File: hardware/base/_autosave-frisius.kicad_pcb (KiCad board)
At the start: 4 copper layers, 46 x 85 mm, 124 parts, among them J1 MEM2067, J2 USB_C_Receptacle_USB2.0, J3 BATTERY, J4 Debug UART, J5 Conn_02x16_Odd_Even_MountingP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, J7 I2C ISENSE, Q2 Q_NMOS_DGS, Q3 Q_NMOS_DGS, SW1 RESET, SW2 BOOT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

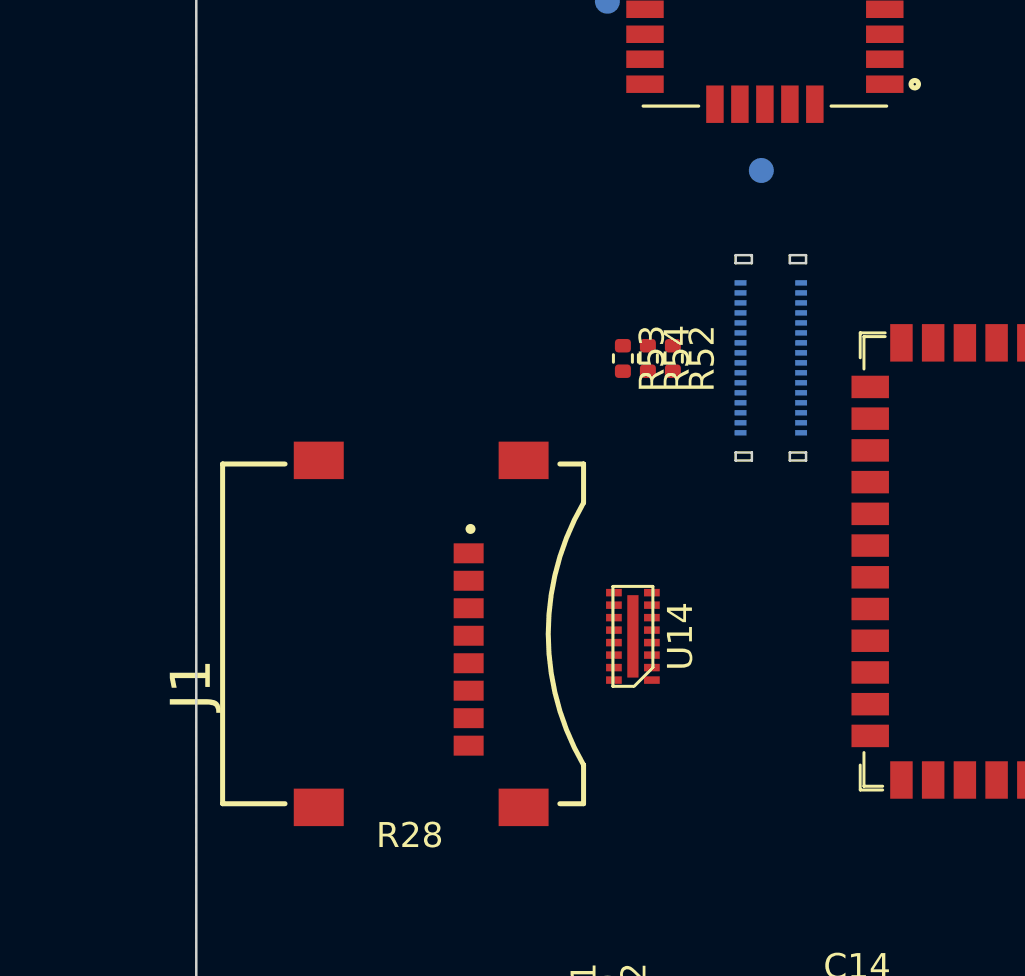
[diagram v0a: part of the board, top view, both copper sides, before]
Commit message: split back out condensed board into lcdboard and base
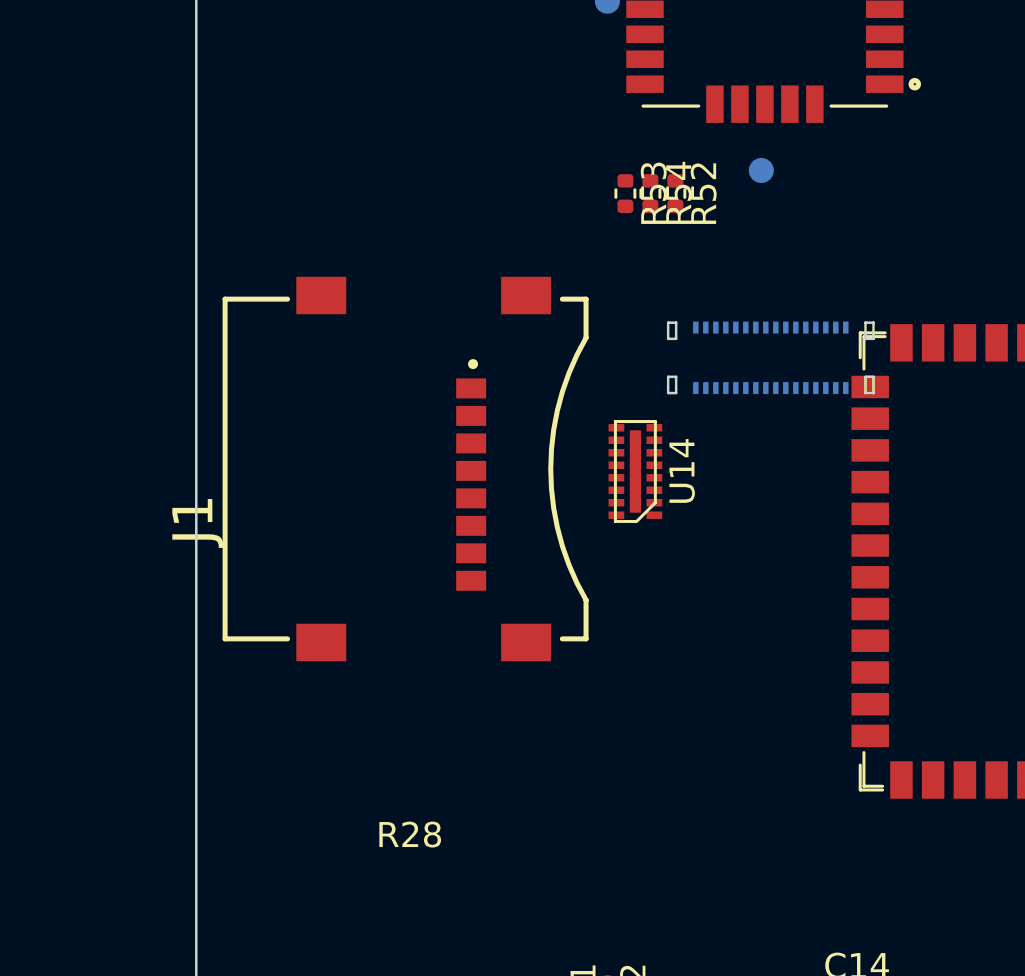
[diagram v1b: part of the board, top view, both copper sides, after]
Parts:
- moved J1 6.60 mm to (60.4, 74.3)
- moved R52 6.60 mm to (71.2, 63.3)
- moved R53 6.60 mm to (69.2, 63.3)
- moved R54 6.60 mm to (70.2, 63.3)
- moved U14 6.60 mm to (69.6, 74.4)
- turned J5 to 0 degrees
